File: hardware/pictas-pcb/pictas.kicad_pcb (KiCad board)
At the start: 2 copper layers, 74.9 x 89.2 mm, 43 parts, among them J1 LED POWER, J10 ICSP_VIZ, J11 CON_RESET, J12 N64 3/4, J13 DSUB1/2, J14 GB, J15 USB Port, J16 VIDEO IN, J17 ICSP_PLAY, J18 SYNC, J19 AUX_FLASH, J2 NES 1/2, J3 VIZ_BOARD_1, J4 VIZ_BOARD_2, J5 VIZ_BOARD_3, J6 VIZ_BOARD_4, J7 AUX_VDD_GND_1, J8 AUX_VDD_GND_2, J9 N64 1/2, Q1 KSC1815_CON_RESET, SW1 MCU_RESET, U1 PIC18F27K42, U2 MCP2221A, U3 PIC18LF47K42, U4 W25Q128JVSIQ, U5 LM1881, U6 TPS2115APWR

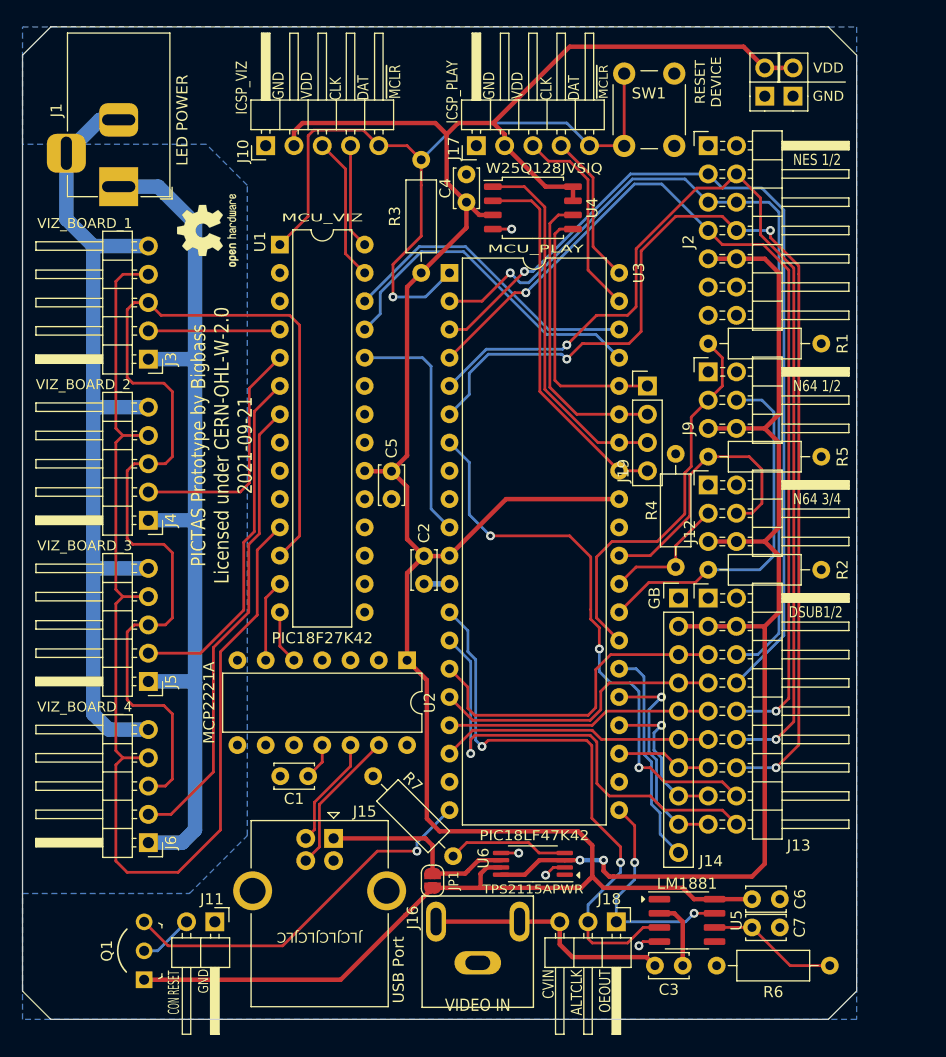
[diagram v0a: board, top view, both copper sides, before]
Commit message: Progress toward replacing pinheaders with D-Sub connector.
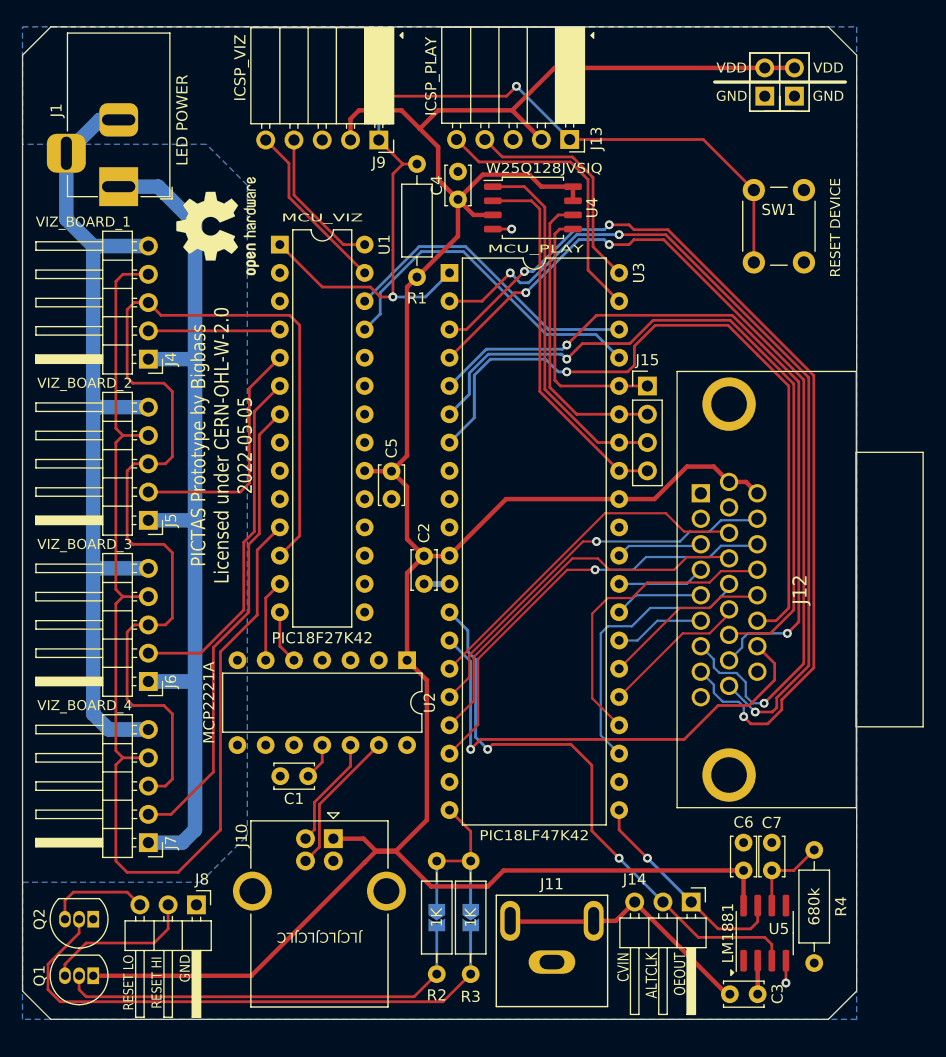
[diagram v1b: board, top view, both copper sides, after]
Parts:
- removed J16: VIDEO IN, pictas:PJRAN1X1U04X
- removed J17: ICSP_PLAY, Connector_PinHeader_2.54mm:PinHeader_1x05_P2.54mm_Horizontal
- removed J18: SYNC, Connector_PinHeader_2.54mm:PinHeader_1x03_P2.54mm_Horizontal
- removed J19: AUX_FLASH, Connector_PinHeader_2.54mm:PinHeader_1x04_P2.54mm_Vertical
- removed R5: 10k, Resistor_THT:R_Axial_DIN0207_L6.3mm_D2.5mm_P10.16mm_Horizontal
- removed R6: 680k, Resistor_THT:R_Axial_DIN0207_L6.3mm_D2.5mm_P10.16mm_Horizontal
- removed R7: 400, Resistor_THT:R_Axial_DIN0207_L6.3mm_D2.5mm_P10.16mm_Horizontal
- removed the REF** at (83.2, 68.6)
- removed U6: TPS2115APWR, Package_SO:TSSOP-8_4.4x3mm_P0.65mm
- added JP2: SolderJumper_2_Open, Jumper:SolderJumper-2_P1.3mm_Open_TrianglePad1.0x1.5mm, B.Cu at (106.8, 130.3)
- added Q2: BC556, Package_TO_SOT_THT:TO-92_Inline, F.Cu at (72.9, 130.4)
- added REF**: OSHW-Logo2_9.8x8mm_SilkScreen, Symbol:OSHW-Logo2_9.8x8mm_SilkScreen, F.Cu at (84.1, 68.2)
- J10: value ICSP_VIZ -> USB Port; footprint Connector_PinHeader_2.54mm:PinHeader_1x05_P2.54mm_Horizontal -> Connector_USB:USB_B_OST_USB-B1HSxx_Horizontal
- J11: value CON_RESET -> VIDEO IN; footprint Connector_PinHeader_2.54mm:PinHeader_1x02_P2.54mm_Horizontal -> pictas:PJRAN1X1U04X
- J12: value N64 3/4 -> CONTROLLER_PORT; footprint Connector_PinHeader_2.54mm:PinHeader_2x03_P2.54mm_Horizontal -> pictas:L77HDA26SD1CH4R
- J13: value DSUB1/2 -> ICSP_PLAY; footprint Connector_PinHeader_2.54mm:PinHeader_2x09_P2.54mm_Horizontal -> Connector_PinSocket_2.54mm:PinSocket_1x05_P2.54mm_Horizontal
- J14: value GB -> SYNC; footprint Connector_PinHeader_2.54mm:PinHeader_1x10_P2.54mm_Vertical -> Connector_PinHeader_2.54mm:PinHeader_1x03_P2.54mm_Horizontal
- J15: value USB Port -> AUX_FLASH; footprint Connector_USB:USB_B_OST_USB-B1HSxx_Horizontal -> Connector_PinHeader_2.54mm:PinHeader_1x04_P2.54mm_Vertical
- J2: value NES 1/2 -> AUX_VDD_GND_1; footprint Connector_PinHeader_2.54mm:PinHeader_2x07_P2.54mm_Horizontal -> Connector_PinHeader_2.54mm:PinHeader_1x02_P2.54mm_Vertical
- J3: value VIZ_BOARD_1 -> AUX_VDD_GND_2; footprint Connector_PinHeader_2.54mm:PinHeader_1x05_P2.54mm_Horizontal -> Connector_PinSocket_2.54mm:PinSocket_1x02_P2.54mm_Vertical
- J4: value VIZ_BOARD_2 -> VIZ_BOARD_1
- J5: value VIZ_BOARD_3 -> VIZ_BOARD_2
- J6: value VIZ_BOARD_4 -> VIZ_BOARD_3
- J7: value AUX_VDD_GND_1 -> VIZ_BOARD_4; footprint Connector_PinHeader_2.54mm:PinHeader_1x02_P2.54mm_Vertical -> Connector_PinHeader_2.54mm:PinHeader_1x05_P2.54mm_Horizontal
- J8: value AUX_VDD_GND_2 -> CON_RESET; footprint Connector_PinSocket_2.54mm:PinSocket_1x02_P2.54mm_Vertical -> Connector_PinHeader_2.54mm:PinHeader_1x03_P2.54mm_Horizontal
- J9: value N64 1/2 -> ICSP_VIZ; footprint Connector_PinHeader_2.54mm:PinHeader_2x03_P2.54mm_Horizontal -> Connector_PinSocket_2.54mm:PinSocket_1x05_P2.54mm_Horizontal
- JP1: value VDD_BYPASS -> SolderJumper_2_Open; footprint Jumper:SolderJumper-2_P1.3mm_Open_RoundedPad1.0x1.5mm -> Jumper:SolderJumper-2_P1.3mm_Open_TrianglePad1.0x1.5mm; moved to B.Cu
- Q1: value KSC1815_CON_RESET -> BC546; footprint digikey-footprints:TO-92-3_Formed_Leads -> Package_TO_SOT_THT:TO-92_Inline
- R1: value 10k -> 10K
- R2: value 10k -> 1K
- R3: value 10K -> 1K
- R4: value 10k -> 680k
- moved J8 88.8 mm to (82.2, 129.2), turned to -90 degrees
- moved J7 88.6 mm to (77.9, 123.6)
- moved R3 63.1 mm to (106.8, 135.4)
- moved J3 62.7 mm to (135.9, 56.5)
- moved J10 62.6 mm to (94.5, 123.2), turned to -90 degrees
- moved R2 50.1 mm to (103.8, 135.4), turned to 90 degrees
- moved J15 49.5 mm to (122.7, 82.5), turned to 0 degrees
- moved J13 43.0 mm to (115.7, 60.4), turned to -90 degrees
- moved R4 37.7 mm to (137.7, 124.2)
- moved R1 36.8 mm to (102.0, 72.8), turned to 90 degrees
- moved J9 36.2 mm to (98.6, 60.5), turned to -90 degrees
- moved J11 30.5 mm to (114.1, 134.3), turned to 0 degrees
- moved J14 27.3 mm to (126.6, 128.9), turned to -90 degrees
- moved SW1 15.7 mm to (136.7, 64.9)
- moved J5 14.5 mm to (77.9, 94.6)
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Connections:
- J10 pad 1: GND -> VDD
- J10 pad 2: VDD -> /D-
- J10 pad 3: Net-(J10-Pad3) -> /D+
- J10 pad 4: Net-(J10-Pad4) -> GND
- J10 pad 5: MCU_RESET -> GND
- J11 pad 1: GND -> /CVIN
- J11 pad 2: Net-(J11-Pad2) -> GND
- J12 pad 1: GND -> unconnected-(J12-Pad1)
- J12 pad 2: GND -> unconnected-(J12-Pad2)
- J12 pad 3: /N64_DATA3 -> /N64_DATA4
- J12 pad 4: /N64_DATA4 -> /N64_DATA3
- J12 pad 5: /3.3V -> /N64_DATA2
- J12 pad 6: /3.3V -> /N64_DATA1
- J13 pad 1: GND -> MCU_RESET
- J13 pad 2: GND -> VDD
- J13 pad 3: /3.3V -> GND
- J13 pad 4: /3.3V -> Net-(J13-Pad4)
- J13 pad 5: /DSUB11 -> Net-(J13-Pad5)
- J14 pad 1: GND -> OEOUT
- J14 pad 2: /3.3V -> ALT_CLK
- J14 pad 3: /DSUB11 -> /CVIN
- J15 pad 1: /USB_5V -> SPI1SDO
- J15 pad 2: /D- -> SPI1SCK
- J15 pad 3: /D+ -> SPI1CS
- J15 pad 4: GND -> SPI1SDI
- J2 pad 2: GND -> VDD
- J3 pad 1: /LED_5V -> GND
- J3 pad 2: /STROBE1 -> VDD
- J4 pad 2: /STROBE2 -> /STROBE1
- J5 pad 2: /STROBE3 -> /STROBE2
- J6 pad 2: /STROBE4 -> /STROBE3
- J7 pad 1: GND -> /LED_5V
- J7 pad 2: VDD -> /STROBE4
- J8 pad 2: VDD -> /RESET_HI
- J9 pad 1: GND -> MCU_RESET
- J9 pad 2: GND -> VDD
- J9 pad 3: /N64_DATA1 -> GND
- J9 pad 4: /N64_DATA2 -> Net-(J9-Pad4)
- J9 pad 5: /3.3V -> Net-(J9-Pad5)
- JP1 pad 1: VDD -> CON_RESET
- JP1 pad 2: /USB_5V -> Net-(JP1-Pad2)
- Q1 pad 2: Net-(J11-Pad2) -> Net-(JP1-Pad2)
- Q1 pad 3: CON_RESET -> /RESET_HI
- R1 pad 1: GND -> VDD
- R1 pad 2: /N64_DATA1 -> MCU_RESET
- R2 pad 1: GND -> Net-(JP1-Pad2)
- R2 pad 2: /N64_DATA2 -> CON_RESET
- R3 pad 1: VDD -> Net-(JP2-Pad2)
- R3 pad 2: MCU_RESET -> CON_RESET
- R4 pad 1: GND -> Net-(C7-Pad2)
- R4 pad 2: /N64_DATA3 -> GND
- U1 pad 24: /UART_HOST -> unconnected-(U1-Pad24)
- U1 pad 27: Net-(J10-Pad3) -> Net-(J9-Pad5)
- U1 pad 28: Net-(J10-Pad4) -> Net-(J9-Pad4)
- U3 pad 10: /UART_HOST -> unconnected-(U3-Pad10)
- U3 pad 14: /DSUB27 -> /DSB7
- U3 pad 15: /DSUB11 -> /GB1/DSA1
- U3 pad 16: /DSUB12 -> /GB2/DSA2
- U3 pad 17: /DSUB13 -> /GB3/DSA3
- U3 pad 18: /DSUB14 -> /GB4/DSA4
- U3 pad 2: /DSUB21 -> /GB9/DSB1/NES_LATCH
- U3 pad 23: /DSUB15 -> /GB5/DSB5
- U3 pad 24: /DSUB16 -> /GB6/DSB6
- U3 pad 25: /DSUB17 -> /GB7/DSB7
- U3 pad 3: /DSUB22 -> /GB10/DSB2/NES_CLK1
- U3 pad 39: Net-(J17-Pad3) -> Net-(J13-Pad5)
- U3 pad 4: /DSUB23 -> /DSB3/NES_DATA1
- U3 pad 40: Net-(J17-Pad4) -> Net-(J13-Pad4)
- U3 pad 5: /DSUB24 -> /DSB4/NES_CLK2
- U3 pad 6: /DSUB25 -> /DSB5/NES_DATA2
- U3 pad 7: /DSUB26 -> /DSB6
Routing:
- net /3.3V: track 106.0 -> 0.00 mm, vias 2 -> 0
- net /DSUB25: track 96.2 -> 0.00 mm, vias 3 -> 0
- net /DSUB24: track 93.9 -> 0.00 mm, vias 2 -> 0
- net /GB10/DSB2/NES_CLK1: track 0.00 -> 84.1 mm, vias 0 -> 3
- net /DSUB23: track 83.8 -> 0.00 mm, vias 2 -> 0
- net /DSUB22: track 81.4 -> 0.00 mm, vias 1 -> 0
- net /DSB3/NES_DATA1: track 0.00 -> 81.3 mm, vias 0 -> 3
- net /DSUB21: track 78.6 -> 0.00 mm, vias 1 -> 0
- net /GB9/DSB1/NES_LATCH: track 0.00 -> 77.1 mm, vias 0 -> 3
- net /DSB4/NES_CLK2: track 0.00 -> 66.2 mm, vias 0 -> 2
- net /DSB5/NES_DATA2: track 0.00 -> 65.3 mm, vias 0 -> 1
- net /DSB6: track 0.00 -> 64.4 mm, vias 0 -> 1
- net Net-(JP2-Pad2): track 0.00 -> 51.3 mm
- net /DSUB26: track 51.3 -> 0.00 mm, vias 3 -> 0
- net /DSB7: track 0.00 -> 44.1 mm, vias 0 -> 1
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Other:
- board text added: "PICTAS Prototype by Bigbass Licensed under CERN-OHL-W-2.0 2022-05-05"
- board text added: "RESET HI"
- board text added: "RESET LO"
- board text removed: "CON RESET"
- board text removed: "PICTAS Prototype by Bigbass Licensed under CERN-OHL-W-2.0 2021-09-21"
